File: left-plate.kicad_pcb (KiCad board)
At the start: 2 copper layers, 155.6 x 97.3 mm, 26 parts

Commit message: rename files
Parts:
- REF** (x26): footprint myles-keyboard:KeyHole -> keyboard:KeyHole
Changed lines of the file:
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@@
   )
   (net 0 "")
-  (footprint "myles-keyboard:KeyHole" (layer "F.Cu")
+  (footprint "keyboard:KeyHole" (layer "F.Cu")
     (at 154.552801 93.512815 -15)
     (fp_text reference "REF**" (at 0 0 -15 unlocked) (layer "F.Fab") hide
@@
       (stroke (width 0.12) (type default)) (fill none) (layer "Edge.Cuts"))
   )
-  (footprint "myles-keyboard:KeyHole" (layer "F.Cu")
+  (footprint "keyboard:KeyHole" (layer "F.Cu")
     (at 119.449871 56.311832 -5)
     (fp_text reference "REF**" (at 0 0 -5 unlocked) (layer "F.Fab") hide
@@
       (stroke (width 0.12) (type default)) (fill none) (layer "Edge.Cuts"))
   )
-  (footprint "myles-keyboard:KeyHole" (layer "F.Cu")
+  (footprint "keyboard:KeyHole" (layer "F.Cu")
     (at 60.145785 103.89932 25)
     (fp_text reference "REF**" (at 0 0 25 unlocked) (layer "F.Fab") hide
@@
       (stroke (width 0.12) (type default)) (fill none) (layer "Edge.Cuts"))
   )
-  (footprint "myles-keyboard:KeyHole" (layer "F.Cu")
+  (footprint "keyboard:KeyHole" (layer "F.Cu")
     (at 134.332871 96.697962 -10)
     (fp_text reference "REF**" (at 0 0 -10 unlocked) (layer "F.Fab") hide
@@
       (stroke (width 0.12) (type default)) (fill none) (layer "Edge.Cuts"))
   )
-  (footprint "myles-keyboard:KeyHole" (layer "F.Cu")
+  (footprint "keyboard:KeyHole" (layer "F.Cu")
     (at 137.28489 79.95623 -10)
     (fp_text reference "REF**" (at 0 0 -10 unlocked) (layer "F.Fab") hide
@@
       (stroke (width 0.12) (type default)) (fill none) (layer "Edge.Cuts"))
   )
-  (footprint "myles-keyboard:KeyHole" (layer "F.Cu")
+  (footprint "keyboard:KeyHole" (layer "F.Cu")
     (at 106.512436 112.397684 -5)
     (fp_text reference "REF**" (at 0 0 -5 unlocked) (layer "F.Fab") hide
@@
       (stroke (width 0.12) (type default)) (fill none) (layer "Edge.Cuts"))
   )
-  (footprint "myles-keyboard:KeyHole" (layer "F.Cu")
+  (footprint "keyboard:KeyHole" (layer "F.Cu")
     (at 176.33939 81.750818 -15)
     (fp_text reference "REF**" (at 0 0 -15 unlocked) (layer "F.Fab") hide
@@
       (stroke (width 0.12) (type default)) (fill none) (layer "Edge.Cuts"))
   )
-  (footprint "myles-keyboard:KeyHole" (layer "F.Cu")
+  (footprint "keyboard:KeyHole" (layer "F.Cu")
     (at 171.939466 98.171557 -15)
     (fp_text reference "REF**" (at 0 0 -15 unlocked) (layer "F.Fab") hide
@@
       (stroke (width 0.12) (type default)) (fill none) (layer "Edge.Cuts"))
   )
-  (footprint "myles-keyboard:KeyHole" (layer "F.Cu")
+  (footprint "keyboard:KeyHole" (layer "F.Cu")
     (at 130.564865 113.295813 -10)
     (fp_text reference "REF**" (at 0 0 -10 unlocked) (layer "F.Fab") hide
@@
       (stroke (width 0.12) (type default)) (fill none) (layer "Edge.Cuts"))
   )
-  (footprint "myles-keyboard:KeyHole" (layer "F.Cu")
+  (footprint "keyboard:KeyHole" (layer "F.Cu")
     (at 116.486576 90.182451 -5)
     (fp_text reference "REF**" (at 0 0 -5 unlocked) (layer "F.Fab") hide
@@
       (stroke (width 0.12) (type default)) (fill none) (layer "Edge.Cuts"))
   )
-  (footprint "myles-keyboard:KeyHole" (layer "F.Cu")
+  (footprint "keyboard:KeyHole" (layer "F.Cu")
     (at 140.236909 63.214498 -10)
     (fp_text reference "REF**" (at 0 0 -10 unlocked) (layer "F.Fab") hide
@@
       (stroke (width 0.12) (type default)) (fill none) (layer "Edge.Cuts"))
   )
-  (footprint "myles-keyboard:KeyHole" (layer "F.Cu")
+  (footprint "keyboard:KeyHole" (layer "F.Cu")
     (at 150.152878 109.933554 -15)
     (fp_text reference "REF**" (at 0 0 -15 unlocked) (layer "F.Fab") hide
@@
       (stroke (width 0.12) (type default)) (fill none) (layer "Edge.Cuts"))
   )
-  (footprint "myles-keyboard:KeyHole" (layer "F.Cu")
+  (footprint "keyboard:KeyHole" (layer "F.Cu")
     (at 79.78 93.5)
     (fp_text reference "REF**" (at 0 0 unlocked) (layer "F.Fab") hide
@@
       (stroke (width 0.12) (type default)) (fill none) (layer "Edge.Cuts"))
   )
-  (footprint "myles-keyboard:KeyHole" (layer "F.Cu")
+  (footprint "keyboard:KeyHole" (layer "F.Cu")
     (at 117.968224 73.247142 -5)
     (fp_text reference "REF**" (at 0 0 -5 unlocked) (layer "F.Fab") hide
@@
       (stroke (width 0.12) (type default)) (fill none) (layer "Edge.Cuts"))
   )
-  (footprint "myles-keyboard:KeyHole" (layer "F.Cu")
+  (footprint "keyboard:KeyHole" (layer "F.Cu")
     (at 97.78 59.5)
     (fp_text reference "REF**" (at 0 0 unlocked) (layer "F.Fab") hide
@@
       (stroke (width 0.12) (type default)) (fill none) (layer "Edge.Cuts"))
   )
-  (footprint "myles-keyboard:KeyHole" (layer "F.Cu")
+  (footprint "keyboard:KeyHole" (layer "F.Cu")
     (at 158.952725 77.092076 -15)
     (fp_text reference "REF**" (at 0 0 -15 unlocked) (layer "F.Fab") hide
@@
       (stroke (width 0.12) (type default)) (fill none) (layer "Edge.Cuts"))
   )
-  (footprint "myles-keyboard:KeyHole" (layer "F.Cu")
+  (footprint "keyboard:KeyHole" (layer "F.Cu")
     (at 67.330295 119.306552 25)
     (fp_text reference "REF**" (at 0 0 25 unlocked) (layer "F.Fab") hide
@@
       (stroke (width 0.12) (type default)) (fill none) (layer "Edge.Cuts"))
   )
-  (footprint "myles-keyboard:KeyHole" (layer "F.Cu")
+  (footprint "keyboard:KeyHole" (layer "F.Cu")
     (at 167.539542 114.592296 -15)
     (fp_text reference "REF**" (at 0 0 -15 unlocked) (layer "F.Fab") hide
@@
       (stroke (width 0.12) (type default)) (fill none) (layer "Edge.Cuts"))
   )
-  (footprint "myles-keyboard:KeyHole" (layer "F.Cu")
+  (footprint "keyboard:KeyHole" (layer "F.Cu")
     (at 86.466581 113.272904 10)
     (fp_text reference "REF**" (at 0 0 10 unlocked) (layer "F.Fab") hide
@@
       (stroke (width 0.12) (type default)) (fill none) (layer "Edge.Cuts"))
   )
-  (footprint "myles-keyboard:KeyHole" (layer "F.Cu")
+  (footprint "keyboard:KeyHole" (layer "F.Cu")
     (at 163.352649 60.671336 -15)
     (fp_text reference "REF**" (at 0 0 -15 unlocked) (layer "F.Fab") hide
@@
       (stroke (width 0.12) (type default)) (fill none) (layer "Edge.Cuts"))
   )
-  (footprint "myles-keyboard:KeyHole" (layer "F.Cu")
+  (footprint "keyboard:KeyHole" (layer "F.Cu")
     (at 97.78 76.5)
     (fp_text reference "REF**" (at 0 0 unlocked) (layer "F.Fab") hide
@@
       (stroke (width 0.12) (type default)) (fill none) (layer "Edge.Cuts"))
   )
-  (footprint "myles-keyboard:KeyHole" (layer "F.Cu")
+  (footprint "keyboard:KeyHole" (layer "F.Cu")
     (at 97.78 93.5)
     (fp_text reference "REF**" (at 0 0 unlocked) (layer "F.Fab") hide
@@
       (stroke (width 0.12) (type default)) (fill none) (layer "Edge.Cuts"))
   )
-  (footprint "myles-keyboard:KeyHole" (layer "F.Cu")
+  (footprint "keyboard:KeyHole" (layer "F.Cu")
     (at 50.124844 130.087443 40)
     (fp_text reference "REF**" (at 0 0 40 unlocked) (layer "F.Fab") hide
@@
       (stroke (width 0.12) (type default)) (fill none) (layer "Edge.Cuts"))
   )
-  (footprint "myles-keyboard:KeyHole" (layer "F.Cu")
+  (footprint "keyboard:KeyHole" (layer "F.Cu")
     (at 79.78 59.5)
     (fp_text reference "REF**" (at 0 0 unlocked) (layer "F.Fab") hide
@@
       (stroke (width 0.12) (type default)) (fill none) (layer "Edge.Cuts"))
   )
-  (footprint "myles-keyboard:KeyHole" (layer "F.Cu")
+  (footprint "keyboard:KeyHole" (layer "F.Cu")
     (at 180.739314 65.330079 -15)
     (fp_text reference "REF**" (at 0 0 -15 unlocked) (layer "F.Fab") hide
@@
       (stroke (width 0.12) (type default)) (fill none) (layer "Edge.Cuts"))
   )
-  (footprint "myles-keyboard:KeyHole" (layer "F.Cu")
+  (footprint "keyboard:KeyHole" (layer "F.Cu")
     (at 79.78 76.5)
     (fp_text reference "REF**" (at 0 0 unlocked) (layer "F.Fab") hide

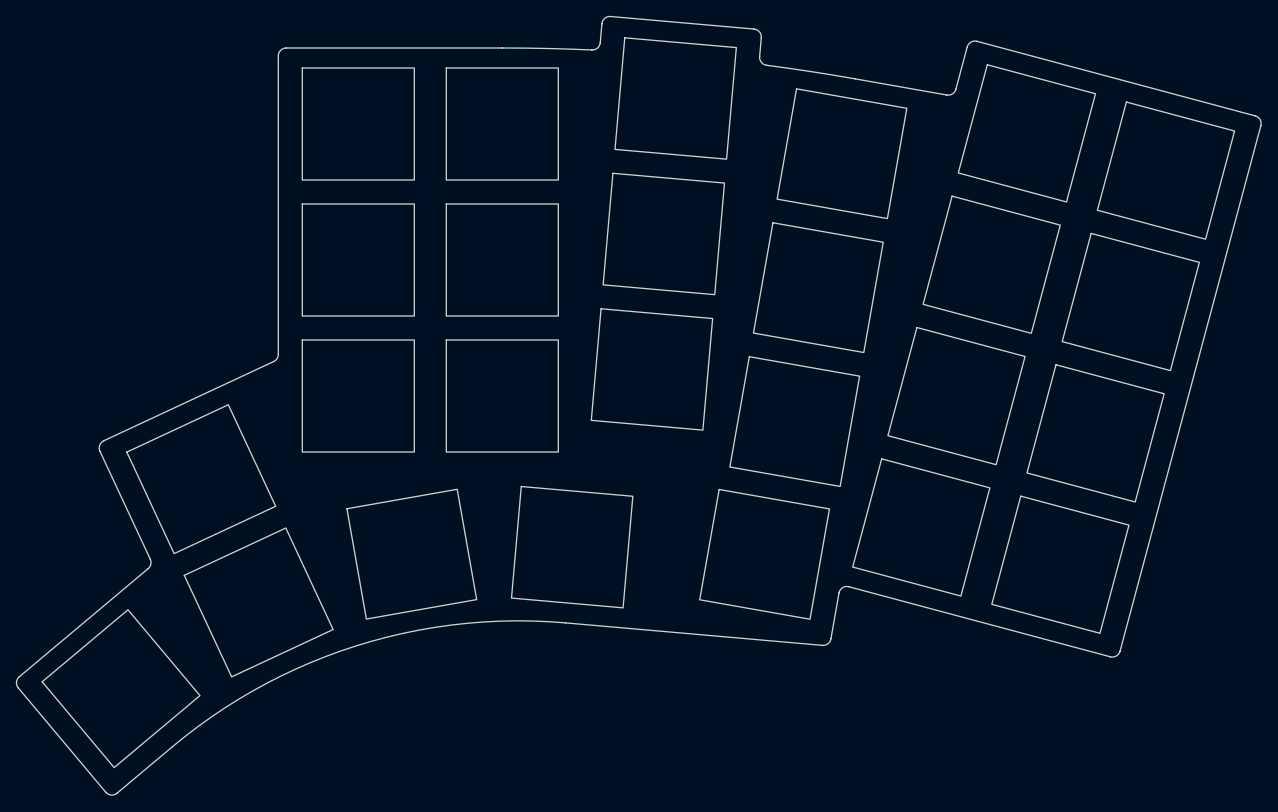
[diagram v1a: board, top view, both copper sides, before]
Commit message: adjust plates and pcb; remove reset button
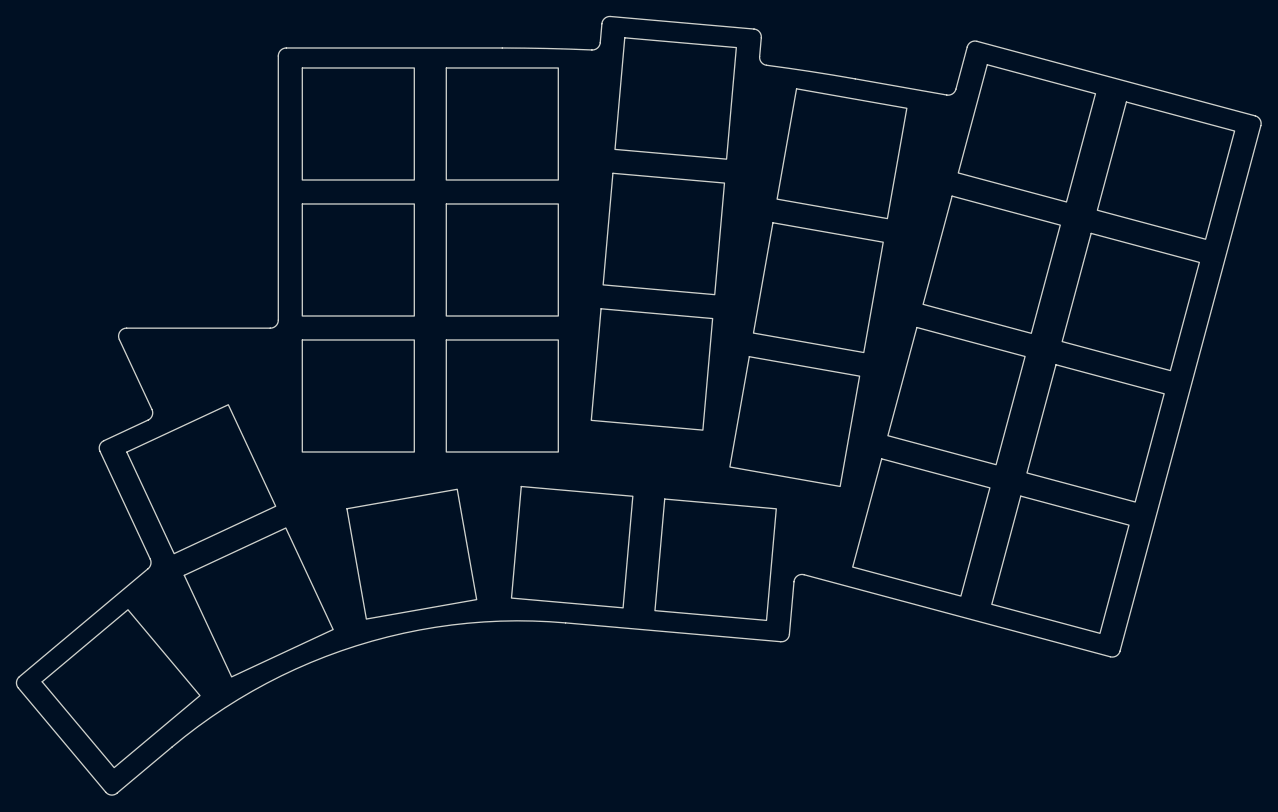
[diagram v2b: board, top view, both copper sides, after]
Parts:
- moved REF** 6.16 mm to (124.4, 114.0), turned to -5 degrees
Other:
- outline, holes or cut-outs redrawn

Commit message: update plates
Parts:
- moved REF** 1.76 mm to (51.5, 128.9)
- moved REF** 1.56 mm to (107.6, 111.3)
- moved REF** 1.56 mm to (68.4, 118.2)
- moved REF** 1.56 mm to (61.2, 102.8)
- moved REF** 1.56 mm to (87.5, 112.1)
- moved REF** 1.54 mm to (125.7, 113.0), turned to -6.171 degrees
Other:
- board size 155.6 x 97.3 mm -> 154.5 x 96.2 mm
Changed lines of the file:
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@@
   )
   (footprint "keyboard:KeyHole" (layer "F.Cu")
-    (at 60.145785 103.89932 25)
+    (at 61.201051 102.753693 25)
     (fp_text reference "REF**" (at 0 0 25 unlocked) (layer "F.Fab") hide
       (effects (font (size 1 1) (thickness 0.1)))
@@
   )
   (footprint "keyboard:KeyHole" (layer "F.Cu")
-    (at 106.512436 112.397684 -5)
+    (at 107.567703 111.252057 -5)
     (fp_text reference "REF**" (at 0 0 -5 unlocked) (layer "F.Fab") hide
       (effects (font (size 1 1) (thickness 0.1)))
@@
   )
   (footprint "keyboard:KeyHole" (layer "F.Cu")
-    (at 124.443941 113.966487 -5)
-    (fp_text reference "REF**" (at 0 0 -5 unlocked) (layer "F.Fab") hide
-      (effects (font (size 1 1) (thickness 0.1)))
-    )
-    (fp_text value "KeyHole" (at 0 2 -5 unlocked) (layer "F.Fab") hide
+    (at 125.654248 113.020897 -6.171)
+    (fp_text reference "REF**" (at 0 0 -6.171 unlocked) (layer "F.Fab") hide
+      (effects (font (size 1 1) (thickness 0.1)))
+    )
+    (fp_text value "KeyHole" (at 0 2 -6.171 unlocked) (layer "F.Fab") hide
       (effects (font (size 1 1) (thickness 0.125)))
     )
@@
   )
   (footprint "keyboard:KeyHole" (layer "F.Cu")
-    (at 67.330295 119.306552 25)
+    (at 68.385562 118.160925 25)
     (fp_text reference "REF**" (at 0 0 25 unlocked) (layer "F.Fab") hide
       (effects (font (size 1 1) (thickness 0.1)))
@@
   )
   (footprint "keyboard:KeyHole" (layer "F.Cu")
-    (at 86.466581 113.272904 10)
+    (at 87.521848 112.127278 10)
     (fp_text reference "REF**" (at 0 0 10 unlocked) (layer "F.Fab") hide
       (effects (font (size 1 1) (thickness 0.1)))
@@
   )
   (footprint "keyboard:KeyHole" (layer "F.Cu")
-    (at 50.124844 130.087443 40)
+    (at 51.462952 128.941816 40)
     (fp_text reference "REF**" (at 0 0 40 unlocked) (layer "F.Fab") hide
       (effects (font (size 1 1) (thickness 0.1)))
@@
     (fp_rect (start -7 -7) (end 7 7) (layer "Edge.Cuts") (stroke (width 0.12) (type default)) (fill none))
   )
-  (gr_arc (start 97.78 50.000001) (mid 103.382237 50.06179) (end 108.981748 50.247128) (layer "Edge.Cuts") (width 0.12))
+  (gr_arc (start 57.569435 136.219239) (mid 80.612677 123.577284) (end 106.739723 120.715907) (layer "Edge.Cuts") (width 0.12))
+  (gr_arc (start 97.78 50) (mid 103.382237 50.061789) (end 108.981748 50.247127) (layer "Edge.Cuts") (width 0.12))
   (gr_arc (start 110.022044 49.335256) (mid 109.685013 50.000098) (end 108.981748 50.247126) (layer "Edge.Cuts") (width 0.12))
-  (gr_line (start 47.490452 100.421886) (end 53.772947 113.894741) (layer "Edge.Cuts") (width 0.12))
+  (gr_line (start 48.545718 99.276259) (end 54.828214 112.749115) (layer "Edge.Cuts") (width 0.12))
   (gr_line (start 69.78 51) (end 69.78 84.02) (layer "Edge.Cuts") (width 0.12))
-  (gr_arc (start 134.24122 116.720205) (mid 134.663841 115.988213) (end 135.496234 115.841441) (layer "Edge.Cuts") (width 0.12))
   (gr_line (start 110.228748 46.972619) (end 110.022044 49.335256) (layer "Edge.Cuts") (width 0.12))
-  (gr_arc (start 53.772946 113.894741) (mid 53.842935 114.533799) (end 53.509427 115.083404) (layer "Edge.Cuts") (width 0.12))
-  (gr_line (start 53.509427 115.083404) (end 37.406804 128.59511) (layer "Edge.Cuts") (width 0.12))
+  (gr_arc (start 55.041575 94.040436) (mid 55.07496 94.805074) (end 54.557885 95.369362) (layer "Edge.Cuts") (width 0.12))
+  (gr_line (start 54.564694 113.937777) (end 38.46207 127.449483) (layer "Edge.Cuts") (width 0.12))
   (gr_line (start 141.886567 53.858826) (end 153.339152 55.878225) (layer "Edge.Cuts") (width 0.12))
   (gr_arc (start 69.78 84.02) (mid 69.487107 84.727107) (end 68.78 85.02) (layer "Edge.Cuts") (width 0.12))
   (gr_arc (start 129.243603 47.632383) (mid 129.922491 47.98579) (end 130.152642 48.715734) (layer "Edge.Cuts") (width 0.12))
-  (gr_line (start 134.24122 116.720205) (end 133.665064 123.305699) (layer "Edge.Cuts") (width 0.12))
+  (gr_line (start 135.17438 116.970262) (end 134.720331 122.160072) (layer "Edge.Cuts") (width 0.12))
   (gr_line (start 174.998839 125.390856) (end 192.598534 59.7079) (layer "Edge.Cuts") (width 0.12))
-  (gr_line (start 53.502619 96.514989) (end 47.974141 99.09296) (layer "Edge.Cuts") (width 0.12))
-  (gr_line (start 173.774094 126.097963) (end 135.496234 115.841441) (layer "Edge.Cuts") (width 0.12))
-  (gr_arc (start 53.986309 95.186063) (mid 54.019693 95.950701) (end 53.502619 96.514989) (layer "Edge.Cuts") (width 0.12))
+  (gr_line (start 54.557885 95.369362) (end 49.029408 97.947333) (layer "Edge.Cuts") (width 0.12))
+  (gr_line (start 173.774094 126.097963) (end 136.429395 116.091481) (layer "Edge.Cuts") (width 0.12))
+  (gr_arc (start 135.17438 116.970262) (mid 135.596995 116.238258) (end 136.429395 116.091481) (layer "Edge.Cuts") (width 0.12))
   (gr_line (start 70.78 50) (end 97.78 50) (layer "Edge.Cuts") (width 0.12))
-  (gr_line (start 132.581714 124.214738) (end 105.684457 121.861533) (layer "Edge.Cuts") (width 0.12))
+  (gr_line (start 133.63698 123.069111) (end 106.739723 120.715906) (layer "Edge.Cuts") (width 0.12))
   (gr_line (start 191.891427 58.483155) (end 157.118097 49.16567) (layer "Edge.Cuts") (width 0.12))
   (gr_arc (start 174.998839 125.390856) (mid 174.532913 125.998062) (end 173.774094 126.097963) (layer "Edge.Cuts") (width 0.12))
-  (gr_arc (start 133.665064 123.305699) (mid 133.311657 123.984588) (end 132.581714 124.214738) (layer "Edge.Cuts") (width 0.12))
   (gr_arc (start 110.228748 46.972619) (mid 110.582155 46.293731) (end 111.312099 46.06358) (layer "Edge.Cuts") (width 0.12))
   (gr_line (start 129.945938 51.07837) (end 130.152642 48.715734) (layer "Edge.Cuts") (width 0.12))
-  (gr_arc (start 47.490452 100.421886) (mid 47.457067 99.657248) (end 47.974141 99.09296) (layer "Edge.Cuts") (width 0.12))
-  (gr_line (start 49.619768 143.149954) (end 56.514168 137.364866) (layer "Edge.Cuts") (width 0.12))
+  (gr_line (start 50.675035 142.004327) (end 57.569435 136.219239) (layer "Edge.Cuts") (width 0.12))
+  (gr_arc (start 50.675034 142.004326) (mid 49.945092 142.234476) (end 49.266203 141.88107) (layer "Edge.Cuts") (width 0.12))
   (gr_line (start 155.893352 49.872776) (end 154.478726 55.152236) (layer "Edge.Cuts") (width 0.12))
-  (gr_line (start 48.210936 143.026697) (end 37.283547 130.003942) (layer "Edge.Cuts") (width 0.12))
+  (gr_arc (start 54.828213 112.749115) (mid 54.898201 113.388172) (end 54.564693 113.937776) (layer "Edge.Cuts") (width 0.12))
+  (gr_line (start 49.266203 141.88107) (end 38.338813 128.858315) (layer "Edge.Cuts") (width 0.12))
   (gr_arc (start 130.812085 52.157035) (mid 130.162398 51.791639) (end 129.945937 51.07837) (layer "Edge.Cuts") (width 0.12))
-  (gr_arc (start 49.619768 143.149954) (mid 48.889825 143.380104) (end 48.210937 143.026696) (layer "Edge.Cuts") (width 0.12))
-  (gr_line (start 53.986308 95.186063) (end 49.909173 86.442618) (layer "Edge.Cuts") (width 0.12))
+  (gr_arc (start 48.545718 99.276259) (mid 48.512333 98.511621) (end 49.029408 97.947333) (layer "Edge.Cuts") (width 0.12))
+  (gr_arc (start 51.498654 86.442618) (mid 51.561571 85.4827) (end 52.404962 85.02) (layer "Edge.Cuts") (width 0.12))
+  (gr_line (start 55.041575 94.040436) (end 51.498654 86.442618) (layer "Edge.Cuts") (width 0.12))
   (gr_arc (start 130.812085 52.157035) (mid 136.358711 52.946858) (end 141.886567 53.858826) (layer "Edge.Cuts") (width 0.12))
-  (gr_line (start 50.815481 85.02) (end 68.78 85.02) (layer "Edge.Cuts") (width 0.12))
+  (gr_arc (start 134.720331 122.160072) (mid 134.366924 122.838961) (end 133.63698 123.069112) (layer "Edge.Cuts") (width 0.12))
+  (gr_line (start 52.404962 85.02) (end 68.78 85.02) (layer "Edge.Cuts") (width 0.12))
   (gr_arc (start 191.891427 58.483155) (mid 192.498633 58.949081) (end 192.598534 59.7079) (layer "Edge.Cuts") (width 0.12))
   (gr_arc (start 69.78 51) (mid 70.072893 50.292893) (end 70.78 50) (layer "Edge.Cuts") (width 0.12))
@@
   (gr_arc (start 155.893352 49.872776) (mid 156.359278 49.26557) (end 157.118097 49.16567) (layer "Edge.Cuts") (width 0.12))
   (gr_arc (start 154.478726 55.152236) (mid 154.050098 55.736805) (end 153.339152 55.878225) (layer "Edge.Cuts") (width 0.12))
-  (gr_arc (start 56.514168 137.364866) (mid 79.55741 124.72291) (end 105.684457 121.861534) (layer "Edge.Cuts") (width 0.12))
-  (gr_arc (start 49.909173 86.442618) (mid 49.97209 85.4827) (end 50.815481 85.02) (layer "Edge.Cuts") (width 0.12))
-  (gr_arc (start 37.283548 130.003941) (mid 37.053398 129.273999) (end 37.406804 128.59511) (layer "Edge.Cuts") (width 0.12))
+  (gr_arc (start 38.338814 128.858315) (mid 38.108663 128.128372) (end 38.46207 127.449483) (layer "Edge.Cuts") (width 0.12))
 )
